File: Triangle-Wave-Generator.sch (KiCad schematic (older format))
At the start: 6 parts

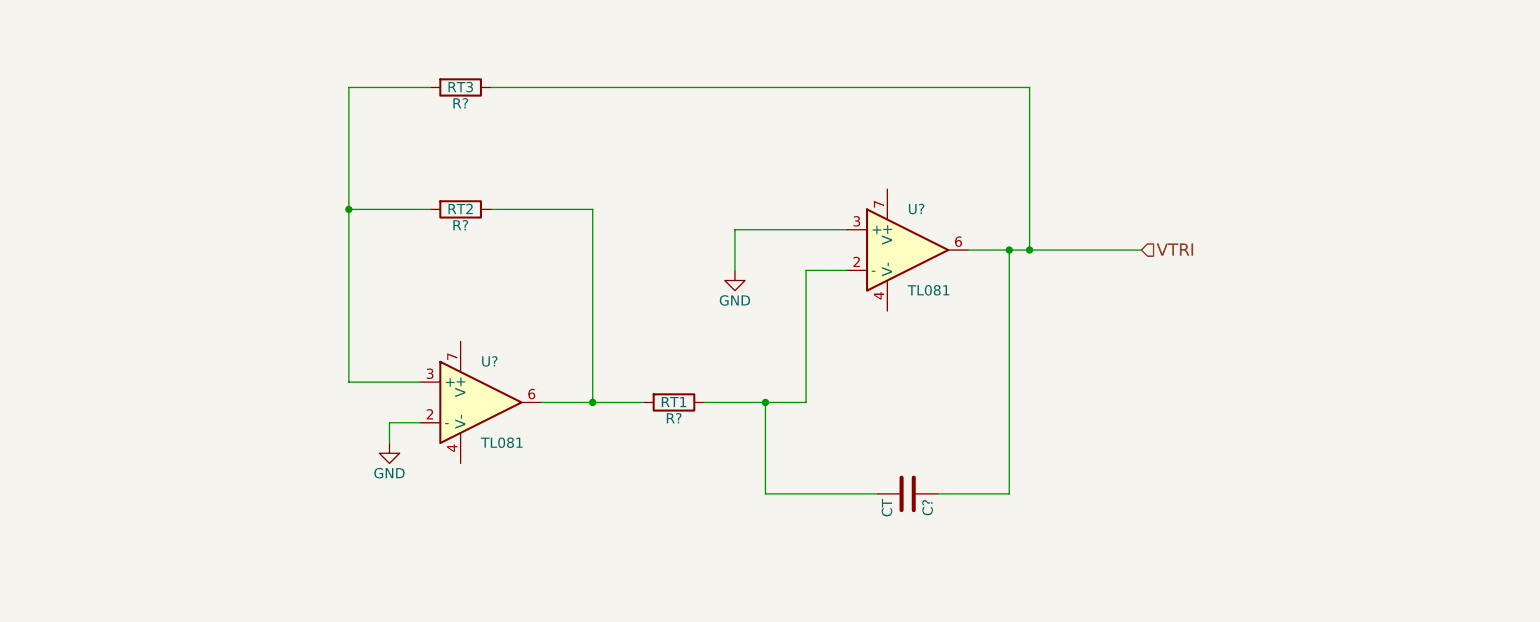
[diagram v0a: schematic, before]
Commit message: Added some markup to the Triangle Wave Generator
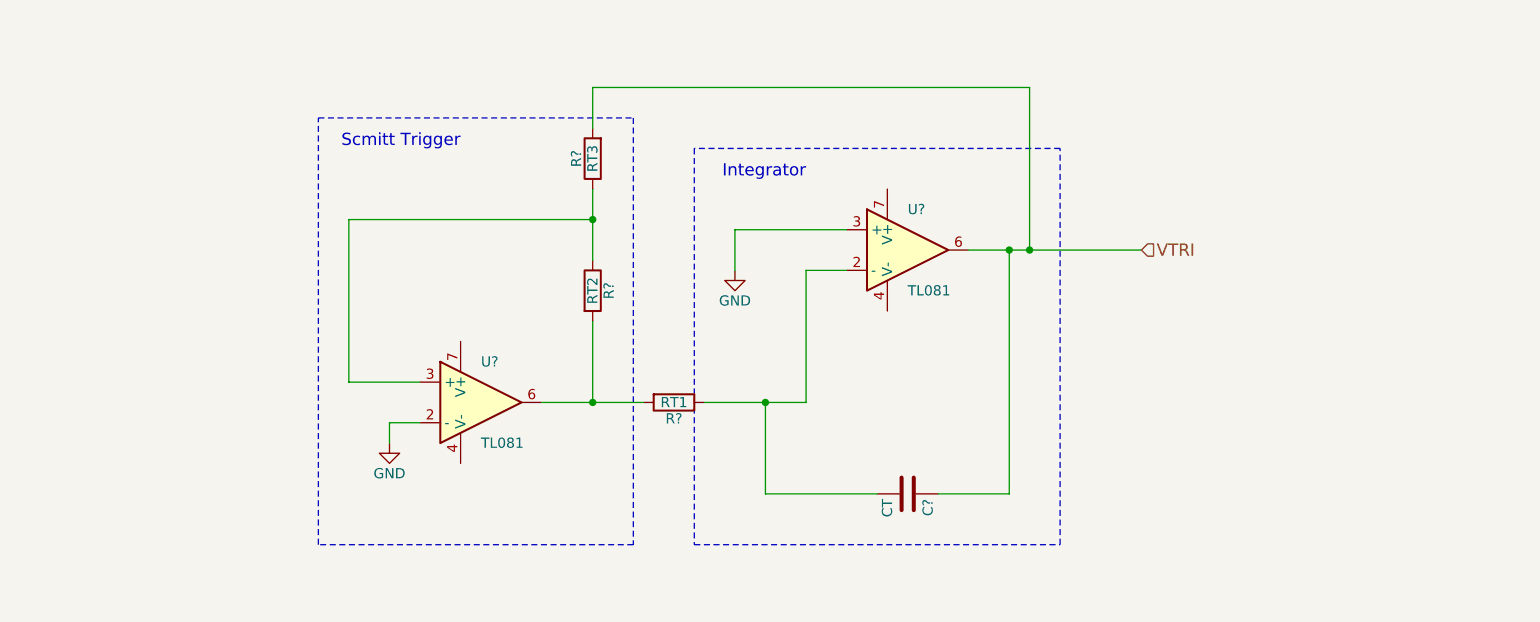
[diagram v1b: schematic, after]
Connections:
- net VTRI: now also R?.2; no longer R?.1
- net at R?.2, U?.6: now also R?.2; no longer R?.1
- new net: R?.1, R?.1, U?.3 (+)
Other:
- note added: "Integrator\n"
- note added: "Scmitt Trigger\n"
- moved on the sheet: R?
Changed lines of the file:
@@
 	1    0    0    -1
 $EndComp
-Wire Wire Line
-	5550 3600 5350 3600
-Wire Wire Line
-	5350 3600 5350 4250
-Wire Wire Line
-	5550 3400 5000 3400
-Wire Wire Line
-	5000 3400 5000 3600
 $Comp
 L GND #PWR?
@@
 	1    0    0    -1
 $EndComp
-Wire Wire Line
-	3300 4450 3300 4350
-Wire Wire Line
-	3300 4350 3450 4350
 $Comp
 L R R?
 U 1 1 58E4F7EA
-P 3650 3300
-F 0 "R?" V 3730 3300 50  0000 C CNN
-F 1 "RT2" V 3650 3300 50  0000 C CNN
-F 2 "" V 3580 3300 50  0000 C CNN
-F 3 "" H 3650 3300 50  0000 C CNN
-	1    3650 3300
-	0    1    1    0
+P 4300 3700
+F 0 "R?" V 4380 3700 50  0000 C CNN
+F 1 "RT2" V 4300 3700 50  0000 C CNN
+F 2 "" V 4230 3700 50  0000 C CNN
+F 3 "" H 4300 3700 50  0000 C CNN
+	1    4300 3700
+	1    0    0    -1
 $EndComp
 $Comp
 L R R?
 U 1 1 58E4F817
-P 3650 2700
-F 0 "R?" V 3730 2700 50  0000 C CNN
-F 1 "RT3" V 3650 2700 50  0000 C CNN
-F 2 "" V 3580 2700 50  0000 C CNN
-F 3 "" H 3650 2700 50  0000 C CNN
-	1    3650 2700
-	0    1    1    0
+P 4300 3050
+F 0 "R?" V 4380 3050 50  0000 C CNN
+F 1 "RT3" V 4300 3050 50  0000 C CNN
+F 2 "" V 4230 3050 50  0000 C CNN
+F 3 "" H 4300 3050 50  0000 C CNN
+	1    4300 3050
+	-1   0    0    1
 $EndComp
 $Comp
@@
 	0    1    1    0
 $EndComp
+Text HLabel 7000 3500 2    60   Input ~ 0
+VTRI
+Wire Wire Line
+	5550 3600 5350 3600
+Wire Wire Line
+	5350 3600 5350 4250
+Wire Wire Line
+	5550 3400 5000 3400
+Wire Wire Line
+	5000 3400 5000 3600
+Wire Wire Line
+	3300 4450 3300 4350
+Wire Wire Line
+	3300 4350 3450 4350
 Wire Wire Line
 	4050 4250 4550 4250
-Wire Wire Line
-	3800 3300 4300 3300
-Wire Wire Line
-	4300 3300 4300 4250
 Connection ~ 4300 4250
 Wire Wire Line
 	3100 4150 3450 4150
-Wire Wire Line
-	3100 2700 3100 4150
-Wire Wire Line
-	3100 3300 3500 3300
-Wire Wire Line
-	3500 2700 3100 2700
-Connection ~ 3100 3300
 Wire Wire Line
 	6150 3500 7000 3500
@@
 Connection ~ 5150 4250
 Wire Wire Line
-	3800 2700 6450 2700
-Wire Wire Line
 	6450 2700 6450 3500
 Connection ~ 6450 3500
-Text HLabel 7000 3500 2    60   Input ~ 0
-VTRI
+Wire Wire Line
+	4300 3850 4300 4250
+Wire Wire Line
+	4300 3550 4300 3200
+Wire Wire Line
+	4300 2900 4300 2700
+Wire Wire Line
+	4300 2700 6450 2700
+Wire Wire Line
+	4300 3350 3100 3350
+Wire Wire Line
+	3100 3350 3100 4150
+Connection ~ 4300 3350
+Wire Notes Line
+	2950 2850 4500 2850
+Wire Notes Line
+	4500 2850 4500 4950
+Wire Notes Line
+	4500 4950 2950 4950
+Wire Notes Line
+	2950 4950 2950 2850
+Text Notes 3650 3000 2    60   ~ 0
+Scmitt Trigger\n
+Wire Notes Line
+	4800 3000 4800 4950
+Wire Notes Line
+	4800 4950 6600 4950
+Wire Notes Line
+	6600 4950 6600 3000
+Wire Notes Line
+	6600 3000 4800 3000
+Text Notes 5350 3150 2    60   ~ 0
+Integrator\n
 $EndSCHEMATC

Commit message: Added the basic Schematic
PWM generators work for given reference design values. (LAB Tested)
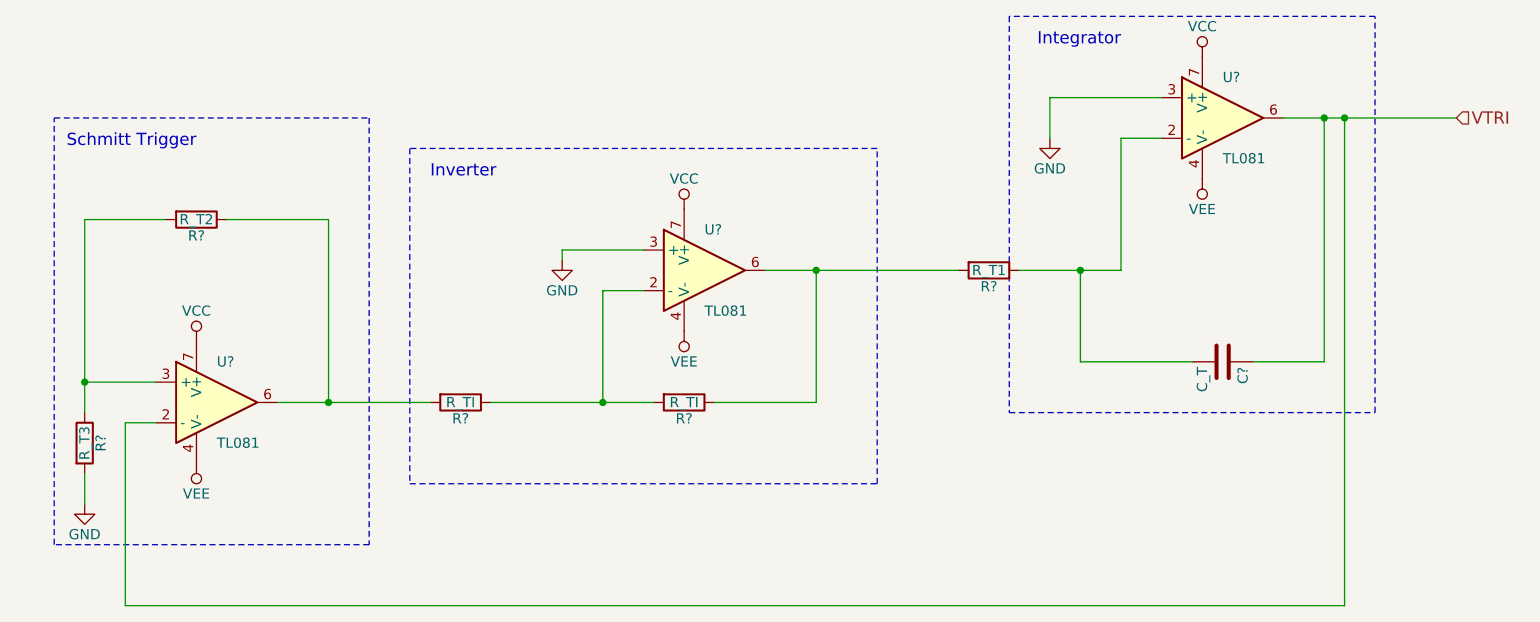
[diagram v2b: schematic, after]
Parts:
- removed R?: RT2, symbol R
- removed R?: RT3, symbol R
- added R?: R_T2, symbol R
- added R?: R_T3, symbol R
- added R? (x2): R_TI, symbol R
- added U?: TL081, symbol TL081
- C?: value CT -> C_T
- R?: value RT1 -> R_T1
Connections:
- net GND: now also R?.2, U?.3 (+); no longer U?.2 (-)
- net VTRI: now also U?.2 (-)
- net VEE: now reaches U?.4 (V-)
- net VEE: now also U?.4 (V-), U?.4 (V-)
- net VCC: now reaches U?.7 (V+)
- net VCC: now also U?.7 (V+), U?.7 (V+)
- net at U?.3 (+): now also R?.1, R?.2
- net at U?.6: now also R?.1, R?.2; no longer R?.2
- new net: R?.1, R?.2, U?.6
- new net: R?.1, R?.2, U?.2 (-)
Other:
- note added: "Inverter"
- note added: "Schmitt Trigger\n"
- note removed: "Scmitt Trigger\n"
- moved on the sheet: C?, R?, U?
